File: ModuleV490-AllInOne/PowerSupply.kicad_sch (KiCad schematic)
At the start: 28 parts, among them J5 POWER_IN, J9 BYPASS, U10 XL7005A, U11 AP2204K-5.0TRG1, U12 XC6206-1.8NR, U9 XC6206-3.3V

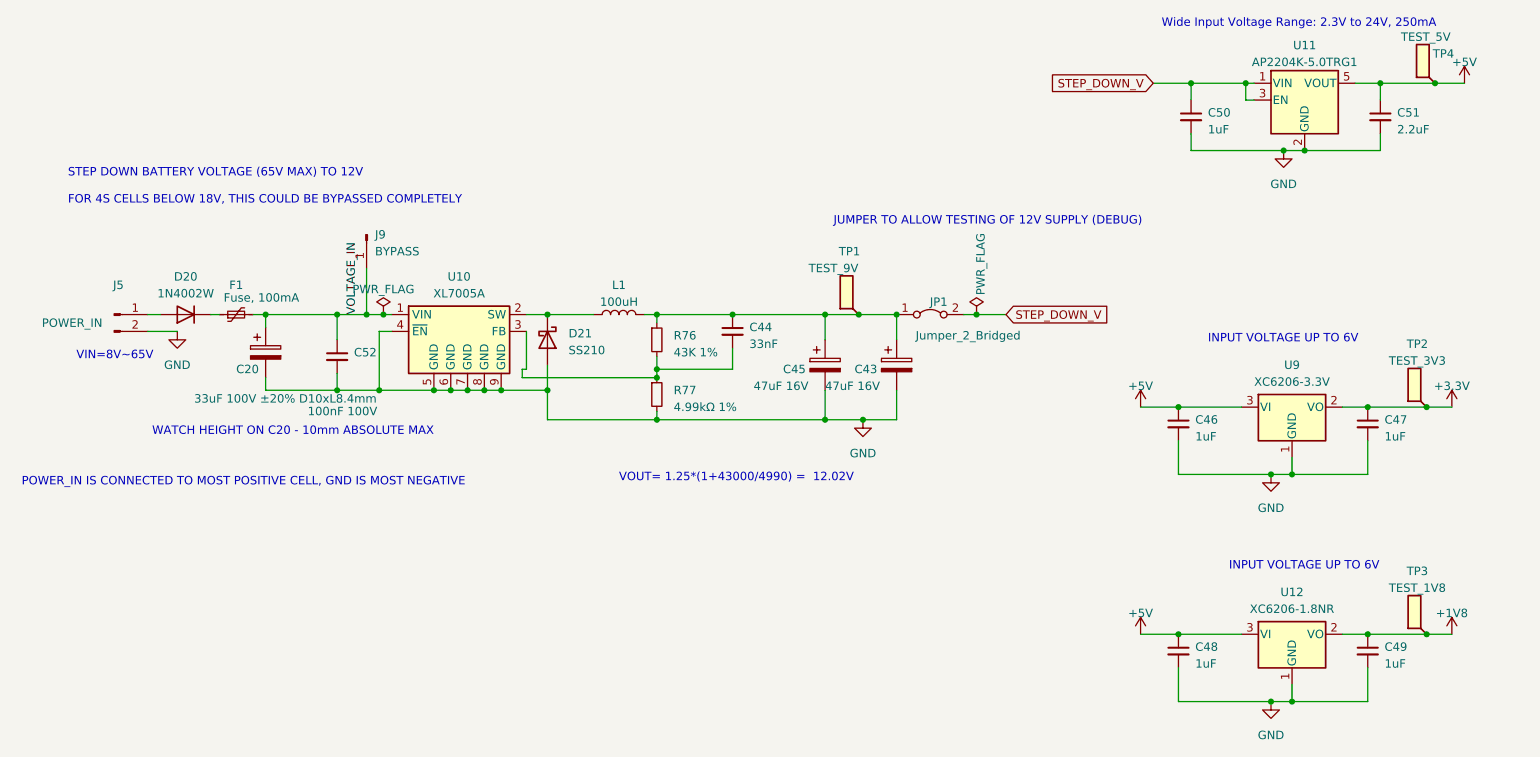
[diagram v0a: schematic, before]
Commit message: Removal JP1 and J9, silkscreen reflects 8S-16S
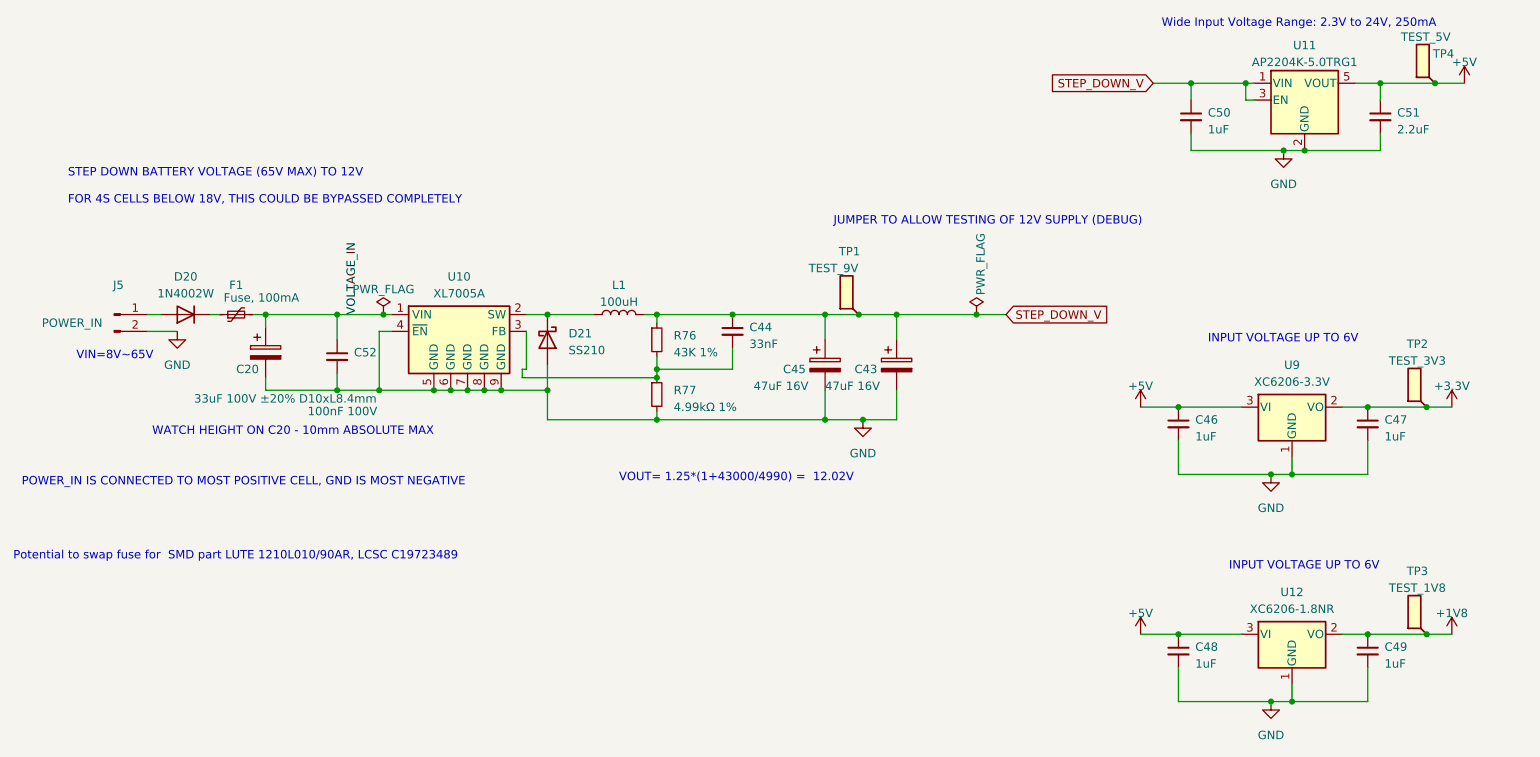
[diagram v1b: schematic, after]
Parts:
- removed J9: BYPASS, Connector_PinSocket_2.54mm:PinSocket_1x01_P2.54mm_Vertical, symbol Connector:Conn_01x01_Pin
- removed JP1: Jumper_2_Bridged, Connector_PinHeader_2.54mm:PinHeader_1x02_P2.54mm_Vertical, symbol Jumper:Jumper_2_Bridged
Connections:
- net STEP_DOWN_V: now also C43.1, C44.1, C45.1, L1.2, R76.1, TP1.1
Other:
- note added: "Potential to swap fuse for SMD part LUTE 1210L010/90AR, LCSC C19723489"
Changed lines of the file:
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@@
   (junction (at 228.6 121.285) (diameter 0) (color 0 0 0 0)
   )
+  (junction (at 210.185 48.26) (diameter 0) (color 0 0 0 0)
+  )
+  (junction (at 64.135 73.025) (diameter 0) (color 0 0 0 0)
+  )
+  (junction (at 208.28 131.445) (diameter 0) (color 0 0 0 0)
+  )
+  (junction (at 64.135 84.455) (diameter 0) (color 0 0 0 0)
+  )
+  (junction (at 205.105 97.155) (diameter 0) (color 0 0 0 0)
+  )
+  (junction (at 112.395 81.28) (diameter 0) (color 0 0 0 0)
+  )
+  (junction (at 70.485 84.455) (diameter 0) (color 0 0 0 0)
+  )
+  (junction (at 78.74 84.455) (diameter 0) (color 0 0 0 0)
+  )
+  (junction (at 201.295 38.1) (diameter 0) (color 0 0 0 0)
+  )
+  (junction (at 88.9 84.455) (diameter 0) (color 0 0 0 0)
+  )
+  (junction (at 191.135 121.285) (diameter 0) (color 0 0 0 0)
+  )
+  (junction (at 219.71 121.285) (diameter 0) (color 0 0 0 0)
+  )
+  (junction (at 71.12 73.025) (diameter 0) (color 0 0 0 0)
+  )
+  (junction (at 53.34 73.025) (diameter 0) (color 0 0 0 0)
+  )
+  (junction (at 143.51 88.9) (diameter 0) (color 0 0 0 0)
+  )
+  (junction (at 137.795 88.9) (diameter 0) (color 0 0 0 0)
+  )
+  (junction (at 112.395 88.9) (diameter 0) (color 0 0 0 0)
+  )
+  (junction (at 123.825 73.025) (diameter 0) (color 0 0 0 0)
+  )
+  (junction (at 228.6 86.995) (diameter 0) (color 0 0 0 0)
+  )
+  (junction (at 142.875 73.025) (diameter 0) (color 0 0 0 0)
+  )
+  (junction (at 95.885 73.025) (diameter 0) (color 0 0 0 0)
+  )
   (junction (at 148.59 73.025) (diameter 0) (color 0 0 0 0)
   )
-  (junction (at 210.185 48.26) (diameter 0) (color 0 0 0 0)
-  )
-  (junction (at 64.135 73.025) (diameter 0) (color 0 0 0 0)
-  )
-  (junction (at 208.28 131.445) (diameter 0) (color 0 0 0 0)
-  )
-  (junction (at 64.135 84.455) (diameter 0) (color 0 0 0 0)
-  )
-  (junction (at 205.105 97.155) (diameter 0) (color 0 0 0 0)
-  )
-  (junction (at 112.395 81.28) (diameter 0) (color 0 0 0 0)
-  )
-  (junction (at 70.485 84.455) (diameter 0) (color 0 0 0 0)
-  )
-  (junction (at 78.74 84.455) (diameter 0) (color 0 0 0 0)
-  )
-  (junction (at 201.295 38.1) (diameter 0) (color 0 0 0 0)
-  )
-  (junction (at 88.9 84.455) (diameter 0) (color 0 0 0 0)
-  )
-  (junction (at 191.135 121.285) (diameter 0) (color 0 0 0 0)
-  )
-  (junction (at 219.71 121.285) (diameter 0) (color 0 0 0 0)
-  )
-  (junction (at 71.12 73.025) (diameter 0) (color 0 0 0 0)
-  )
-  (junction (at 68.58 73.025) (diameter 0) (color 0 0 0 0)
-  )
-  (junction (at 53.34 73.025) (diameter 0) (color 0 0 0 0)
-  )
-  (junction (at 143.51 88.9) (diameter 0) (color 0 0 0 0)
-  )
-  (junction (at 137.795 88.9) (diameter 0) (color 0 0 0 0)
-  )
-  (junction (at 112.395 88.9) (diameter 0) (color 0 0 0 0)
-  )
-  (junction (at 123.825 73.025) (diameter 0) (color 0 0 0 0)
-  )
-  (junction (at 228.6 86.995) (diameter 0) (color 0 0 0 0)
-  )
-  (junction (at 142.875 73.025) (diameter 0) (color 0 0 0 0)
-  )
-  (junction (at 95.885 73.025) (diameter 0) (color 0 0 0 0)
-  )
   (junction (at 137.795 73.025) (diameter 0) (color 0 0 0 0)
   )
+  (junction (at 160.655 73.025) (diameter 0) (color 0 0 0 0)
+  )
   (junction (at 221.615 38.1) (diameter 0) (color 0 0 0 0)
   )
@@
   (junction (at 112.395 73.025) (diameter 0) (color 0 0 0 0)
   )
-  (junction (at 160.655 73.025) (diameter 0) (color 0 0 0 0)
-  )
   (junction (at 219.71 86.995) (diameter 0) (color 0 0 0 0)
   )
@@
     (stroke (width 0) (type default))
   )
-  (wire (pts (xy 68.58 73.025) (xy 71.12 73.025))
-    (stroke (width 0) (type default))
-  )
   (wire (pts (xy 53.34 84.455) (xy 64.135 84.455))
     (stroke (width 0) (type default))
@@
     (stroke (width 0) (type default))
   )
-  (wire (pts (xy 158.75 73.025) (xy 160.655 73.025))
-    (stroke (width 0) (type default))
-  )
   (wire (pts (xy 207.01 48.26) (xy 210.185 48.26))
     (stroke (width 0) (type default))
@@
     (stroke (width 0) (type default))
   )
-  (wire (pts (xy 68.58 66.04) (xy 68.58 73.025))
-    (stroke (width 0) (type default))
-  )
   (wire (pts (xy 70.485 75.565) (xy 70.485 84.455))
     (stroke (width 0) (type default))
@@
     (stroke (width 0) (type default))
   )
-  (wire (pts (xy 64.135 73.025) (xy 68.58 73.025))
+  (wire (pts (xy 64.135 73.025) (xy 71.12 73.025))
     (stroke (width 0) (type default))
   )
@@
   )
   (wire (pts (xy 53.34 73.025) (xy 64.135 73.025))
+    (stroke (width 0) (type default))
+  )
+  (wire (pts (xy 148.59 73.025) (xy 160.655 73.025))
     (stroke (width 0) (type default))
   )
@@
   )
   (text "Wide Input Voltage Range: 2.3V to 24V, 250mA" (at 188.595 29.845 0)
+    (effects (font (size 1.27 1.27)) (justify left bottom))
+  )
+  (text "Potential to swap fuse for  SMD part LUTE 1210L010/90AR, LCSC C19723489"
+    (at 15.24 110.236 0)
     (effects (font (size 1.27 1.27)) (justify left bottom))
   )
@@
         (path "/e63e39d7-6ac0-4ffd-8aa3-1841a4541b55/8dad0a00-271a-4077-b7a7-daab5ad043ac"
           (reference "C52") (unit 1)
-        )
-      )
-    )
-  )
-  (symbol (lib_id "Jumper:Jumper_2_Bridged") (at 153.67 73.025 0) (unit 1)
-    (in_bom yes) (on_board yes) (dnp no)
-    (property "Reference" "JP1" (at 154.94 71.12 0)
-      (effects (font (size 1.27 1.27)))
-    )
-    (property "Value" "Jumper_2_Bridged" (at 159.385 76.2 0)
-      (effects (font (size 1.27 1.27)))
-    )
-    (property "Footprint" "Connector_PinHeader_2.54mm:PinHeader_1x02_P2.54mm_Vertical" (at 153.67 73.025 0)
-      (effects (font (size 1.27 1.27)) hide)
-    )
-    (property "Datasheet" "~" (at 153.67 73.025 0)
-      (effects (font (size 1.27 1.27)) hide)
-    )
-    (property "PartNumber" "DZ254R-11-02-63" (at 153.67 73.025 0)
-      (effects (font (size 1.27 1.27)) hide)
-    )
-    (property "LCSCStockCode" "C2935908" (at 153.67 73.025 0)
-      (effects (font (size 1.27 1.27)) hide)
-    )
-    (pin "1")
-    (pin "2")
-    (instances
-      (project "Module_16S"
-        (path "/e63e39d7-6ac0-4ffd-8aa3-1841a4541b55/8dad0a00-271a-4077-b7a7-daab5ad043ac"
-          (reference "JP1") (unit 1)
         )
       )
@@
         )
       )
-    )
-  )
-  (symbol (lib_id "Connector:Conn_01x01_Pin") (at 68.58 60.96 270) (unit 1)
-    (in_bom no) (on_board yes) (dnp no) (fields_autoplaced)
-    (property "Reference" "J9" (at 69.85 60.96 90)
-      (effects (font (size 1.27 1.27)) (justify left))
-    )
-    (property "Value" "BYPASS" (at 69.85 63.5 90)
-      (effects (font (size 1.27 1.27)) (justify left))
-    )
-    (property "Footprint" "Connector_PinSocket_2.54mm:PinSocket_1x01_P2.54mm_Vertical" (at 68.58 60.96 0)
-      (effects (font (size 1.27 1.27)) hide)
-    )
-    (property "Datasheet" "~" (at 68.58 60.96 0)
-      (effects (font (size 1.27 1.27)) hide)
-    )
-    (pin "1")
-    (instances
-      (project "Module_16S"
-        (path "/e63e39d7-6ac0-4ffd-8aa3-1841a4541b55/8dad0a00-271a-4077-b7a7-daab5ad043ac"
-          (reference "J9") (unit 1)
-        )
-      )

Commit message: 14pF caps to 0402 parts (stock availability)
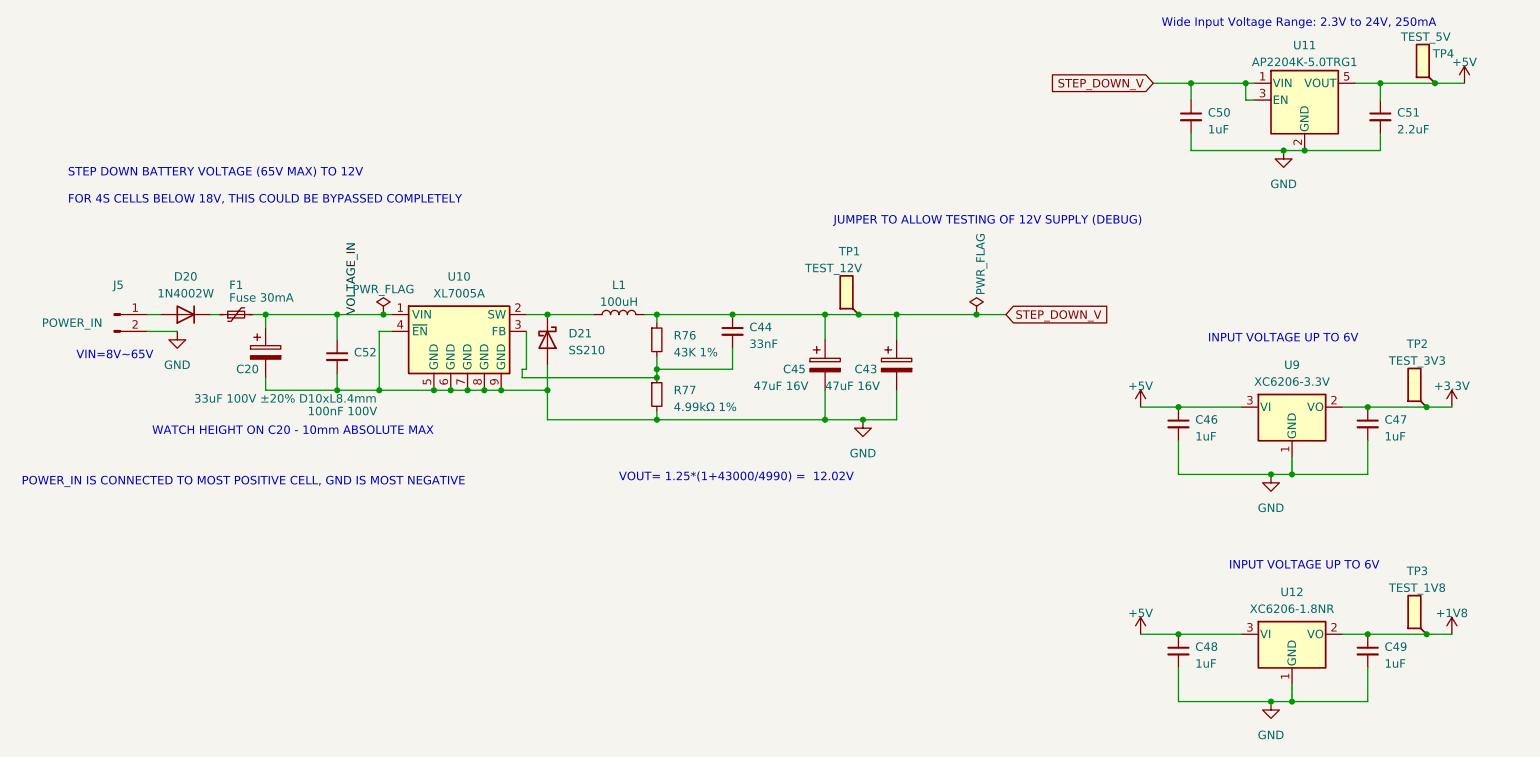
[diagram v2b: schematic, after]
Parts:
- F1: value Fuse, 100mA -> Fuse 30mA; footprint Fuse:Fuse_Bourns_MF-RHT100 -> Fuse:Fuse_0805_2012Metric; LCSCStockCode C2680606 -> C19273358; PartNumber JK250-100U -> 0805L003/80XR
- TP1: value TEST_9V -> TEST_12V
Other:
- note removed: "Potential to swap fuse for SMD part LUTE 1210L010/90AR, LCSC C19723489"
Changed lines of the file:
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@@
-    (effects (font (size 1.27 1.27)) (justify left bottom))
-  )
-  (text "Potential to swap fuse for  SMD part LUTE 1210L010/90AR, LCSC C19723489"
-    (at 15.24 110.236 0)
     (effects (font (size 1.27 1.27)) (justify left bottom))
   )
@@
       (effects (font (size 1.27 1.27)))
     )
-    (property "Value" "Fuse, 100mA" (at 52.705 70.485 90)
-      (effects (font (size 1.27 1.27)))
-    )
-    (property "Footprint" "Fuse:Fuse_Bourns_MF-RHT100" (at 53.975 71.755 0)
+    (property "Value" "Fuse 30mA" (at 52.705 70.485 90)
+      (effects (font (size 1.27 1.27)))
+    )
+    (property "Footprint" "Fuse:Fuse_0805_2012Metric" (at 53.975 71.755 0)
       (effects (font (size 1.27 1.27)) (justify left) hide)
     )
-    (property "Datasheet" "https://datasheet.lcsc.com/lcsc/2304140030_Jinrui-Electronic-Materials-Co--JK250-100U_C2680606.pdf" (at 48.895 73.025 0)
-      (effects (font (size 1.27 1.27)) hide)
-    )
-    (property "PartNumber" "JK250-100U" (at 48.895 73.025 90)
-      (effects (font (size 1.27 1.27)) hide)
-    )
-    (property "LCSCStockCode" "C2680606" (at 48.895 73.025 0)
+    (property "Datasheet" "https://wmsc.lcsc.com/wmsc/upload/file/pdf/v2/lcsc/2312012005_LUTE-0805L003-80XR_C19273358.pdf" (at 48.895 73.025 0)
+      (effects (font (size 1.27 1.27)) hide)
+    )
+    (property "PartNumber" "0805L003/80XR" (at 48.895 73.025 90)
+      (effects (font (size 1.27 1.27)) hide)
+    )
+    (property "LCSCStockCode" "C19273358" (at 48.895 73.025 0)
       (effects (font (size 1.27 1.27)) hide)
     )
@@
       (effects (font (size 1.27 1.27)))
     )
-    (property "Value" "TEST_9V" (at 139.065 66.04 90)
-      (effects (font (size 1.27 1.27)))
-    )
+    (property "Value" "TEST_12V" (at 139.065 66.04 90)
+      (effects (font (size 1.27 1.27)))
+    )

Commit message: Inductor part change - fix workflows
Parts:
- L1: footprint COILMX:MS1040-101M -> Inductor_SMD:L_1008_2520Metric_Pad1.43x2.20mm_HandSolder; LCSCStockCode C380060 -> C286551; PartNumber MS1040-101M -> NLV25T-101J-EF
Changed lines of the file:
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@@
       (effects (font (size 1.27 1.27)))
     )
-    (property "Footprint" "COILMX:MS1040-101M" (at 106.68 73.025 0)
+    (property "Footprint" "Inductor_SMD:L_1008_2520Metric_Pad1.43x2.20mm_HandSolder" (at 106.68 73.025 0)
       (effects (font (size 1.27 1.27)) hide)
     )
@@
       (effects (font (size 1.27 1.27)) hide)
     )
-    (property "PartNumber" "MS1040-101M" (at 106.68 73.025 0)
+    (property "PartNumber" "NLV25T-101J-EF" (at 106.68 73.025 0)
       (effects (font (size 1.27 1.27)) hide)
     )
-    (property "LCSCStockCode" "C380060" (at 106.68 73.025 0)
+    (property "LCSCStockCode" "C286551" (at 106.68 73.025 0)
       (effects (font (size 1.27 1.27)) hide)
     )
